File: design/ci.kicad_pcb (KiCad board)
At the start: 2 copper layers, 21.4 x 18.5 mm, 2 parts

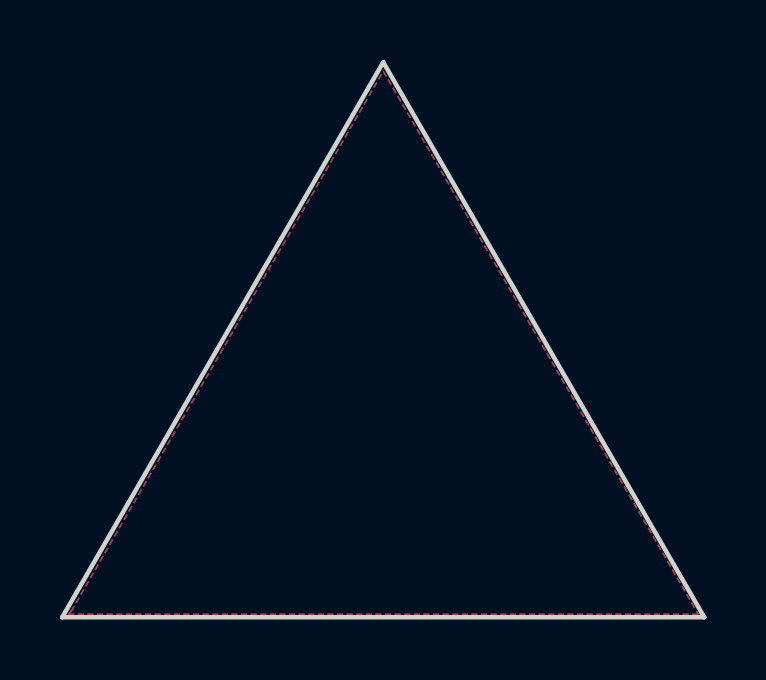
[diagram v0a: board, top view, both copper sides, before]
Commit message: [enh] Update with solder pad behind
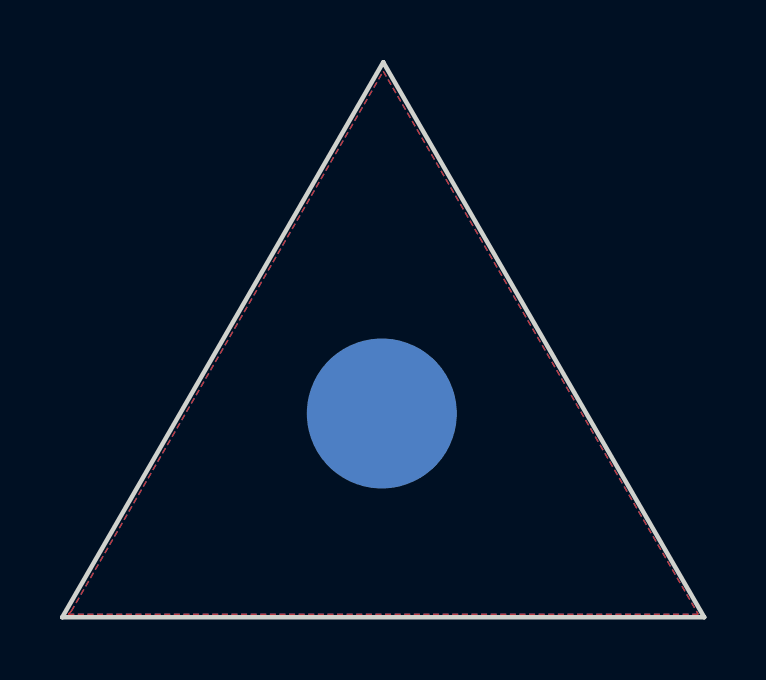
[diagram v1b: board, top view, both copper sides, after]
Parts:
- added REF**: pad, pad, B.Cu at (136.7, 102.1)
- moved G*** 6.23 mm to (136.7, 96.3), turned to 0 degrees
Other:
- board text added: "Sex and Chopes"
